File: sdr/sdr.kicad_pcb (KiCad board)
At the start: 4 copper layers, 85 x 53 mm, 98 parts, among them J1 USB_C_Receptacle_USB2.0, J2 Conn_01x06, J3 Conn_Coaxial, J4 PJ-320D, J5 Screen, Q5 AO3400A, Q6 AO3401A, SW1 RESET, SW2 KEY, SW3 PTT, U1 AMS1117-3.3, U10 BGA2817, U11 74LVC1G66, U12 74LVC1G66, U13 74LVC1G66, U14 74LVC1G66, U2 MS5351M, U3 LM4871M/TR, U4 CH32V305RBT6, U5 BGA2817, U6 GS8091-TR, U7 74LVC1G66, U8 FM1630C, Y1 25MHz, Y2 25MHz

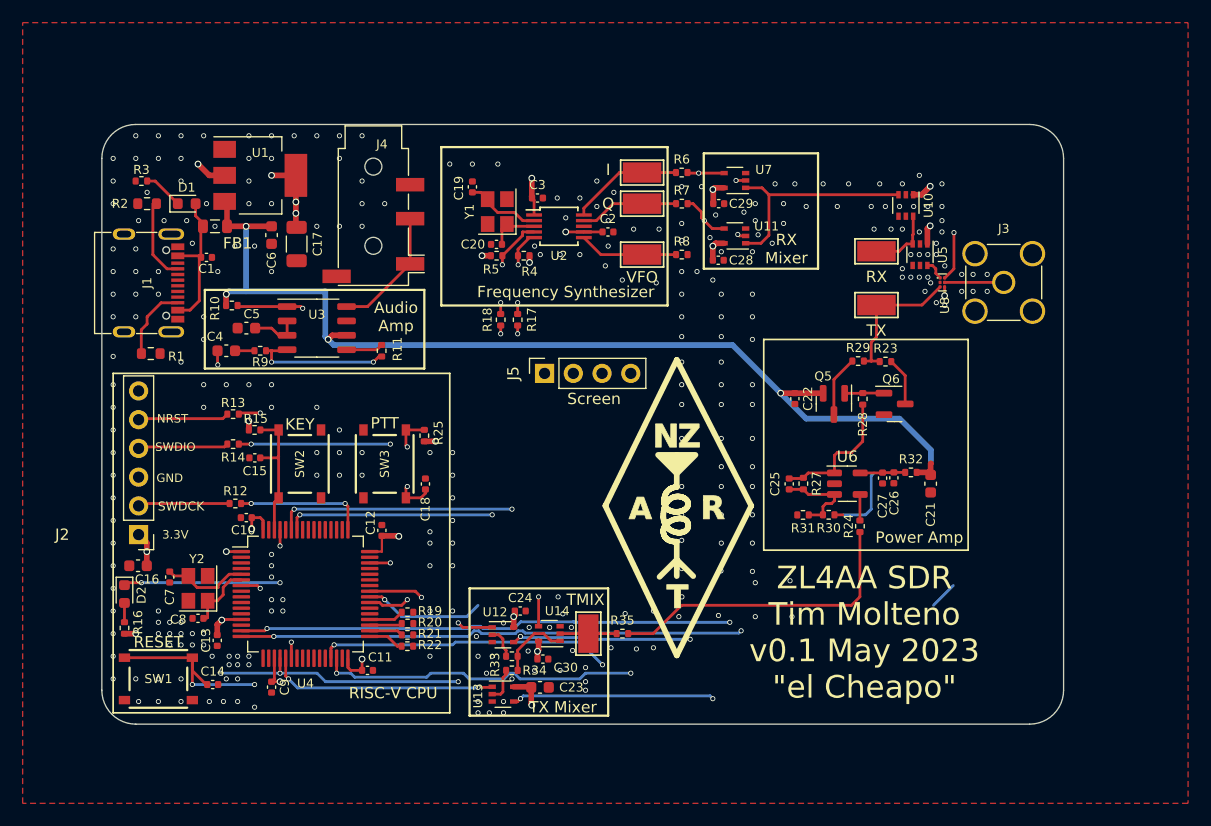
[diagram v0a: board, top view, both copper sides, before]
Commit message: Update footprints, and add an swd-connect-5
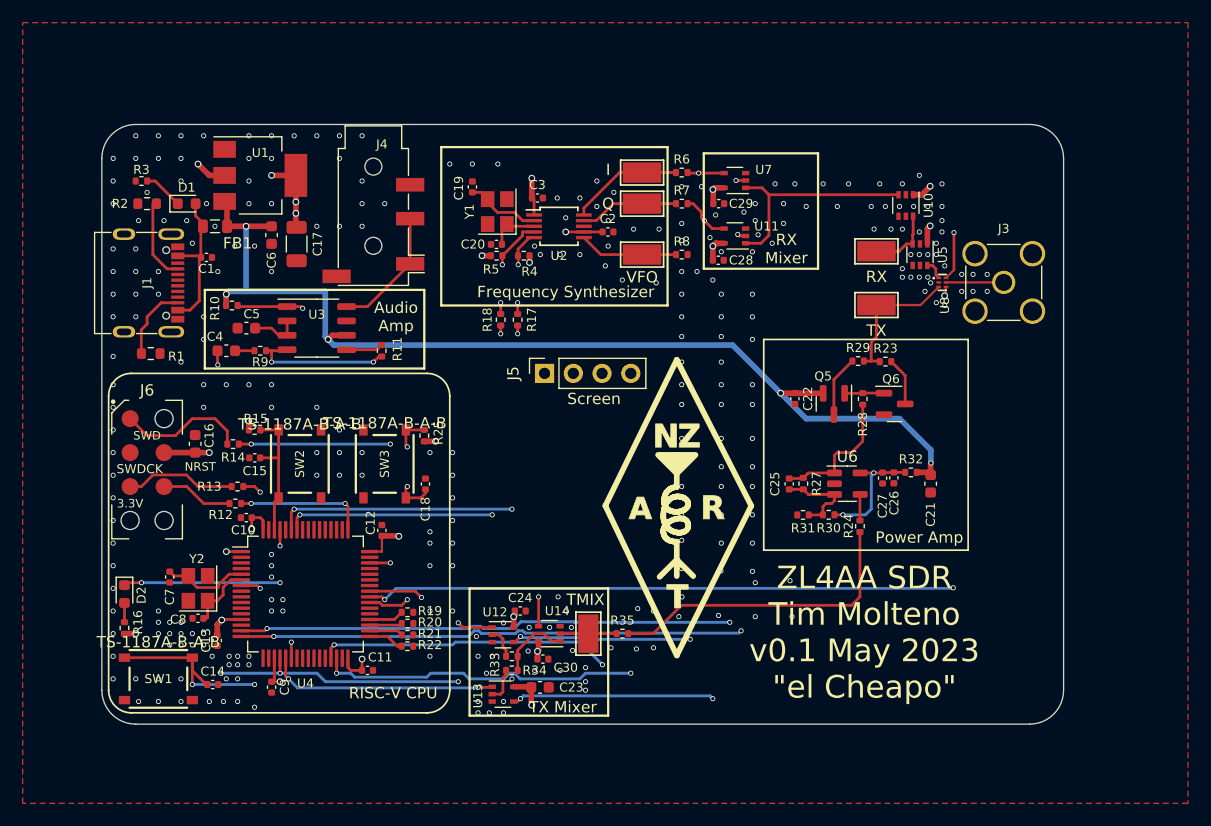
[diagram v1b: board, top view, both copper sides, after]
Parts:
- removed J2: Conn_01x06, Connector_PinHeader_2.54mm:PinHeader_1x06_P2.54mm_Vertical
- added J6: swd-connect-5, swd-connect:swd-connect-5-mcu, F.Cu at (123.0, 94.5)
- D2: value LED -> PB8
- SW1: value RESET -> TS-1187A-B-A-B
- SW2: value KEY -> TS-1187A-B-A-B
- SW3: value PTT -> TS-1187A-B-A-B
- U3: value LM4871M/TR -> LM4871M/TR_C383075
- moved C16 11.9 mm to (127.2, 92.2), turned to 90 degrees
- moved R13 6.41 mm to (131.0, 96.0)
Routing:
- net RX_EN: track 48.8 -> 87.8 mm, vias 2 -> 3
- net NRST: track 44.5 -> 37.5 mm
- net Net-(J6-SWD): track 8.00 -> 11.4 mm
- net Net-(J6-RST): track 7.92 -> 9.83 mm
- net Net-(J6-SWCLK): track 8.13 -> 6.41 mm
- net +3.3V: track 56.1 -> 57.1 mm
- net +5V: track 92.6 -> 92.5 mm, vias 4 -> 5
- net +5P: vias 0 -> 2
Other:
- board text added: "SWD"
- board text removed: "GND"
- board text removed: "SWDIO"
